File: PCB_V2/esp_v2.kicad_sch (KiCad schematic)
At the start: 13 parts, among them J2 Conn_01x03_Socket, J3 Screw_Terminal_01x02, U1 ESP-32S

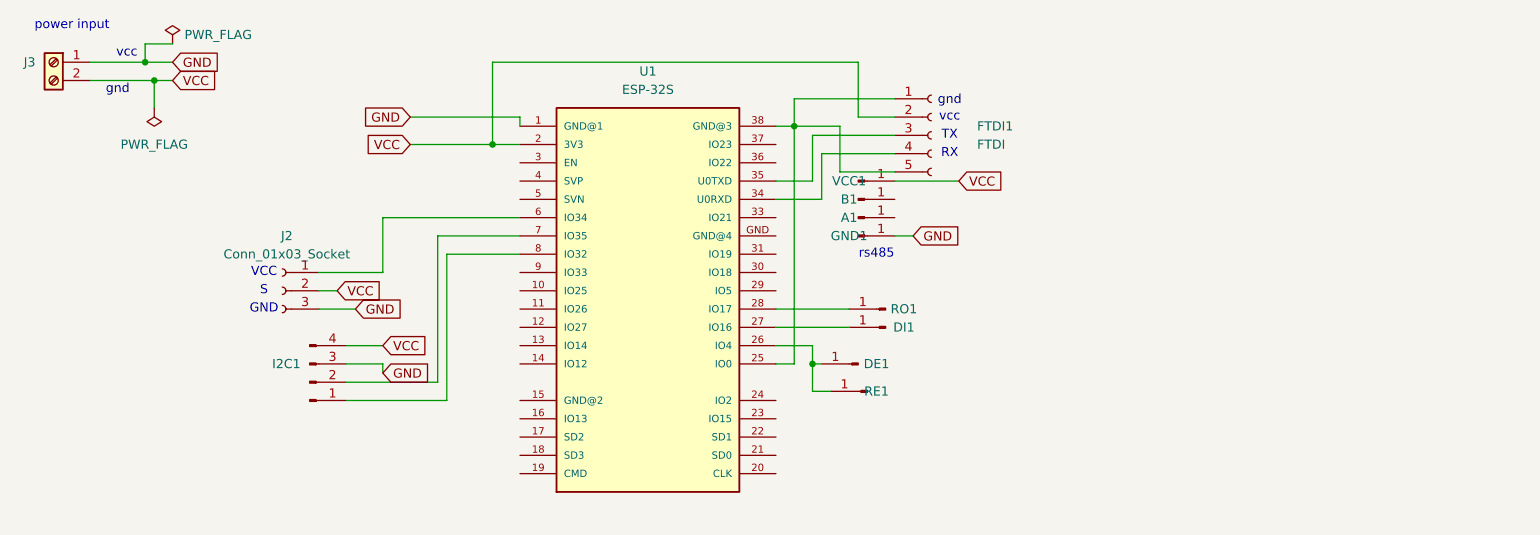
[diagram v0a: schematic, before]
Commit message: expanded tracks' width
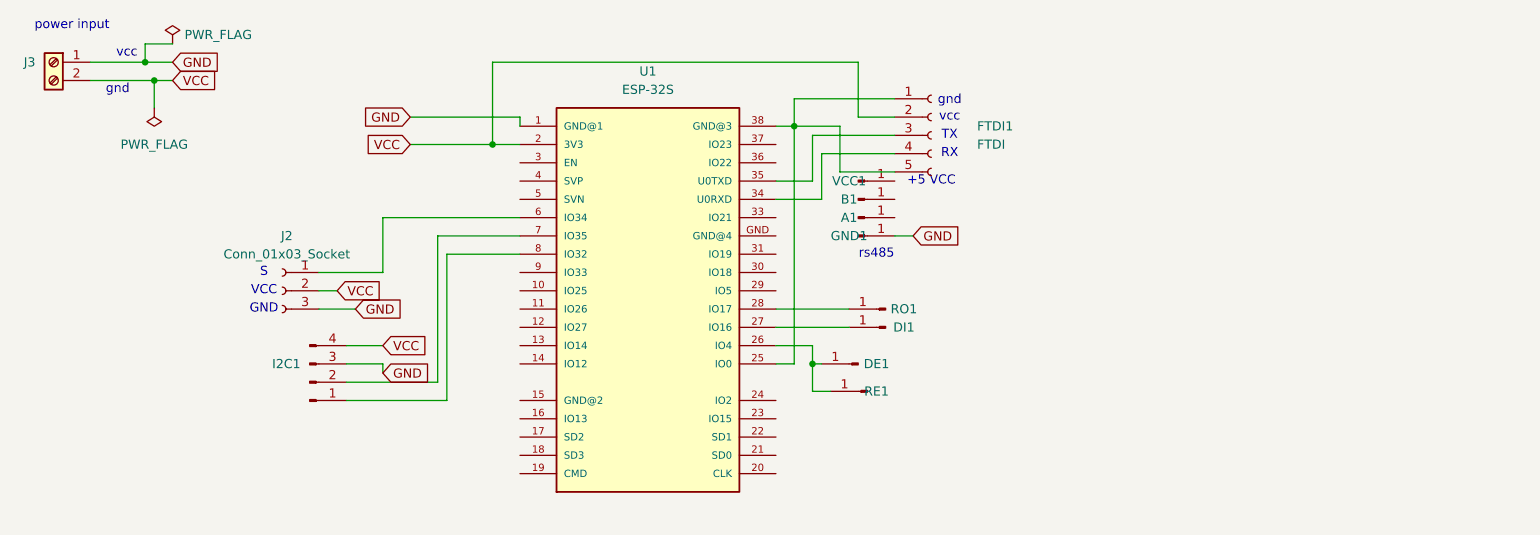
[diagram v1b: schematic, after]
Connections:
- net VCC: no longer VCC1.1 (Pin_1)
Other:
- note added: "+5 VCC"
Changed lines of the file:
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@@
 	(generator_version "9.0")
 	(paper "A4")
-	(text "VCC\n"
+	(text "S"
 		(exclude_from_sim no)
 		(at 50.8 48.26 0)
@@
 		)
 	)
-	(text "S\n"
+	(text "+5 VCC"
+		(exclude_from_sim no)
+		(at 143.51 35.56 0)
+		(effects
+			(font
+				(size 1.27 1.27)
+			)
+		)
+	)
+	(text "VCC"
 		(exclude_from_sim no)
 		(at 50.8 50.8 0)
@@
 	(wire
 		(pts
-			(xy 138.43 35.56) (xy 147.32 35.56)
-		)
-		(stroke
-			(width 0)
-			(type default)
-		)
-	)
-	(wire
-		(pts
 			(xy 38.1 16.51) (xy 34.29 16.51)
 		)
@@
 				(hide yes)
 			)
-		)
-	)
-	(global_label "VCC"
-		(shape input)
-		(at 147.32 35.56 0)
-		(fields_autoplaced yes)
-		(effects
-			(font
-				(size 1.27 1.27)
-			)
-			(justify left)
-		)
-		(property "Intersheetrefs" "${INTERSHEET_REFS}"
-			(at 153.9338 35.56 0)
-			(effects
-				(font
-					(size 1.27 1.27)
-				)
-				(justify left)
-				(hide yes)
-			)

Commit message: After our first etching we reiliaze pins were too small . SO we had toenlearge them.
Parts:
- A1, B1, DE1, GND1, RE1, RO1, VCC1: footprint Connector_PinHeader_1.00mm:PinHeader_1x01_P1.00mm_Vertical -> Connector_PinHeader_2.54mm:PinHeader_1x01_P2.54mm_Vertical
- FTDI1: footprint Connector_PinSocket_1.00mm:PinSocket_1x05_P1.00mm_Vertical -> Connector_PinSocket_2.54mm:PinSocket_1x05_P2.54mm_Vertical
- I2C1: footprint Connector_PinHeader_1.00mm:PinHeader_1x04_P1.00mm_Vertical -> Connector_PinHeader_2.54mm:PinHeader_1x04_P2.54mm_Vertical
- J2: footprint Connector_PinSocket_1.00mm:PinSocket_1x03_P1.00mm_Vertical -> Connector_PinSocket_2.54mm:PinSocket_1x03_P2.54mm_Vertical
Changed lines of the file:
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@@
 			)
 		)
-		(property "Footprint" "Connector_PinHeader_1.00mm:PinHeader_1x01_P1.00mm_Vertical"
+		(property "Footprint" "Connector_PinHeader_2.54mm:PinHeader_1x01_P2.54mm_Vertical"
 			(at 134.62 64.77 0)
 			(effects
@@
 			)
 		)
-		(property "Footprint" "Connector_PinHeader_1.00mm:PinHeader_1x01_P1.00mm_Vertical"
+		(property "Footprint" "Connector_PinHeader_2.54mm:PinHeader_1x01_P2.54mm_Vertical"
 			(at 133.35 40.64 0)
 			(effects
@@
 			)
 		)
-		(property "Footprint" "Connector_PinHeader_1.00mm:PinHeader_1x01_P1.00mm_Vertical"
+		(property "Footprint" "Connector_PinHeader_2.54mm:PinHeader_1x01_P2.54mm_Vertical"
 			(at 133.35 60.96 0)
 			(effects
@@
 			)
 		)
-		(property "Footprint" "Connector_PinHeader_1.00mm:PinHeader_1x04_P1.00mm_Vertical"
+		(property "Footprint" "Connector_PinHeader_2.54mm:PinHeader_1x04_P2.54mm_Vertical"
 			(at 57.15 63.5 0)
 			(effects
@@
 			)
 		)
-		(property "Footprint" "Connector_PinHeader_1.00mm:PinHeader_1x01_P1.00mm_Vertical"
+		(property "Footprint" "Connector_PinHeader_2.54mm:PinHeader_1x01_P2.54mm_Vertical"
 			(at 133.35 35.56 0)
 			(effects
@@
 			)
 		)
-		(property "Footprint" "Connector_PinSocket_1.00mm:PinSocket_1x05_P1.00mm_Vertical"
+		(property "Footprint" "Connector_PinSocket_2.54mm:PinSocket_1x05_P2.54mm_Vertical"
 			(at 143.51 29.21 0)
 			(effects
@@
 			)
 		)
-		(property "Footprint" "Connector_PinHeader_1.00mm:PinHeader_1x01_P1.00mm_Vertical"
+		(property "Footprint" "Connector_PinHeader_2.54mm:PinHeader_1x01_P2.54mm_Vertical"
 			(at 133.35 43.18 0)
 			(effects
@@
 			)
 		)
-		(property "Footprint" "Connector_PinHeader_1.00mm:PinHeader_1x01_P1.00mm_Vertical"
+		(property "Footprint" "Connector_PinHeader_2.54mm:PinHeader_1x01_P2.54mm_Vertical"
 			(at 133.35 38.1 0)
 			(effects
@@
 			)
 		)
-		(property "Footprint" "Connector_PinSocket_1.00mm:PinSocket_1x03_P1.00mm_Vertical"
+		(property "Footprint" "Connector_PinSocket_2.54mm:PinSocket_1x03_P2.54mm_Vertical"
 			(at 53.34 50.8 0)
 			(effects
@@
 			)
 		)
-		(property "Footprint" "Connector_PinHeader_1.00mm:PinHeader_1x01_P1.00mm_Vertical"
+		(property "Footprint" "Connector_PinHeader_2.54mm:PinHeader_1x01_P2.54mm_Vertical"
 			(at 137.16 53.34 0)
 			(effects

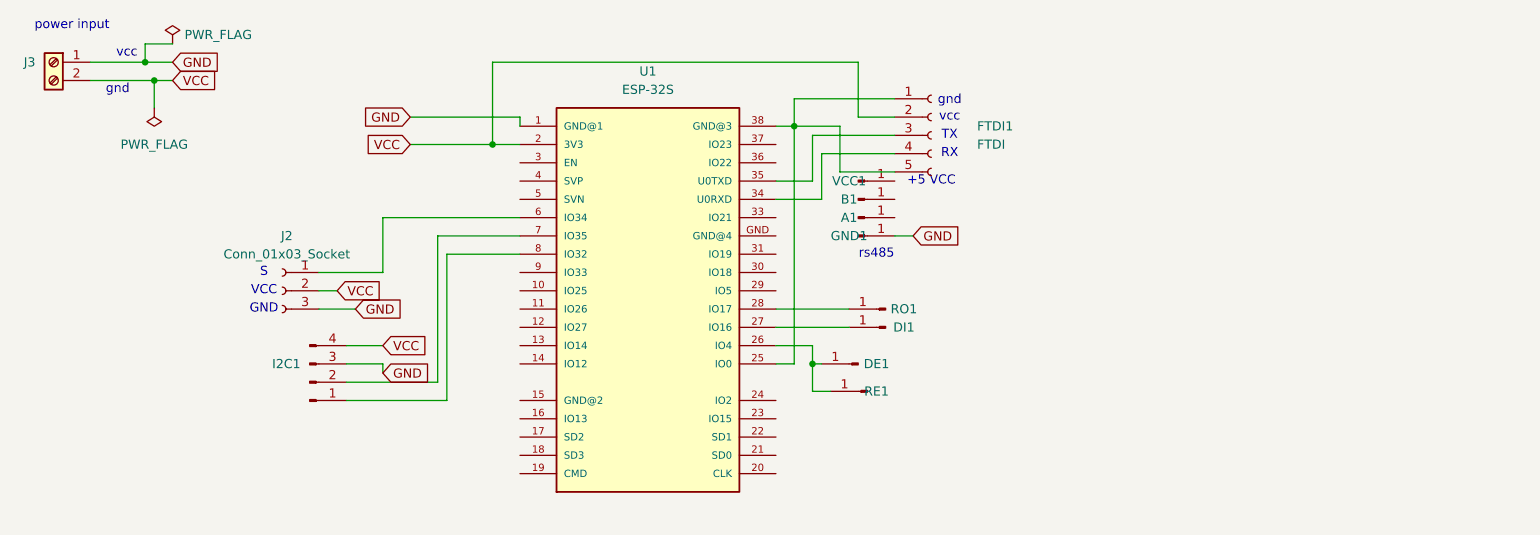
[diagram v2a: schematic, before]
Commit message: correction on I2C for the lcd
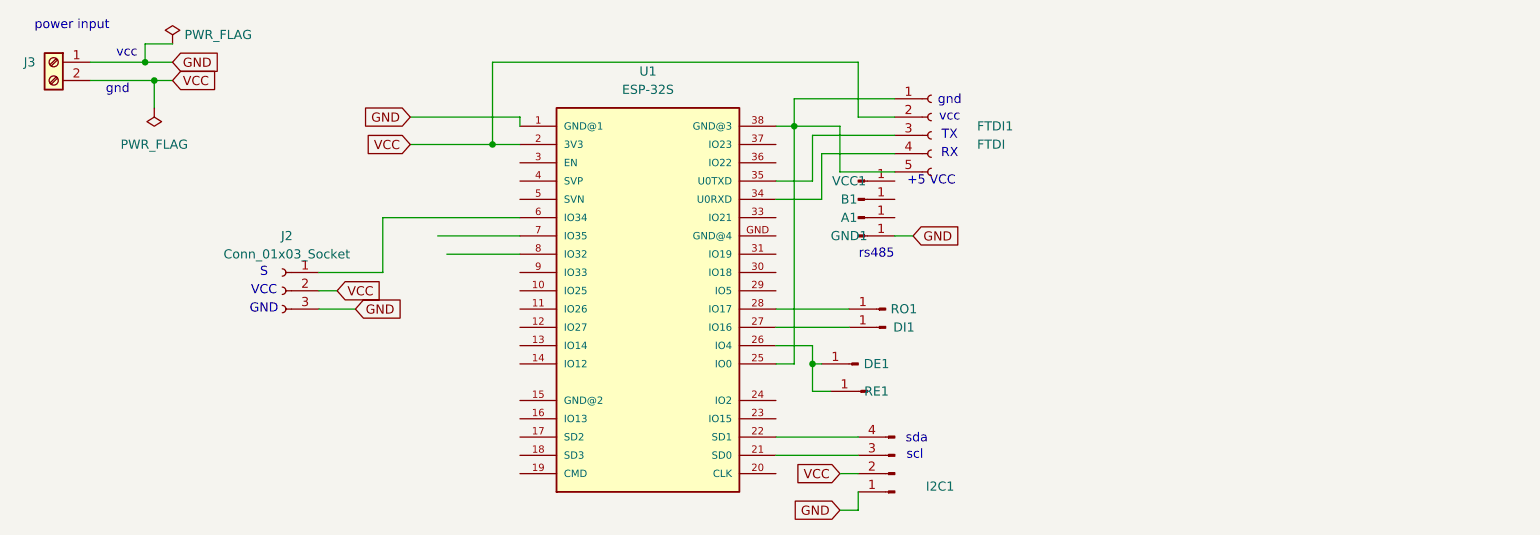
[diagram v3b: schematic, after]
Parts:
- DI1: footprint Connector_PinHeader_1.00mm:PinHeader_1x01_P1.00mm_Vertical -> Connector_PinHeader_2.54mm:PinHeader_1x01_P2.54mm_Vertical
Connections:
- net GND: now also I2C1.1 (Pin_1); no longer I2C1.3 (Pin_3)
- net VCC: now also I2C1.2 (Pin_2); no longer I2C1.4 (Pin_4)
- net at U1.21 (SD0): now also I2C1.3 (Pin_3)
- net at U1.22 (SD1): now also I2C1.4 (Pin_4)
- net at U1.7 (IO35): no longer I2C1.2 (Pin_2)
- net at U1.8 (IO32): no longer I2C1.1 (Pin_1)
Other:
- note added: "scl"
- note added: "sda"
- moved on the sheet: I2C1
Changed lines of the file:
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@@
 	(generator_version "9.0")
 	(paper "A4")
+	(text "sda"
+		(exclude_from_sim no)
+		(at 141.478 71.374 0)
+		(effects
+			(font
+				(size 1.27 1.27)
+			)
+		)
+	)
 	(text "S"
 		(exclude_from_sim no)
@@
 		(exclude_from_sim no)
 		(at 146.05 26.67 0)
+		(effects
+			(font
+				(size 1.27 1.27)
+			)
+		)
+	)
+	(text "scl\n"
+		(exclude_from_sim no)
+		(at 141.224 73.66 0)
 		(effects
 			(font
@@
 	(wire
 		(pts
+			(xy 121.92 73.66) (xy 133.35 73.66)
+		)
+		(stroke
+			(width 0)
+			(type default)
+		)
+	)
+	(wire
+		(pts
 			(xy 26.67 21.59) (xy 35.56 21.59)
 		)
@@
 	(wire
 		(pts
+			(xy 130.81 76.2) (xy 133.35 76.2)
+		)
+		(stroke
+			(width 0)
+			(type default)
+		)
+	)
+	(wire
+		(pts
 			(xy 67.31 40.64) (xy 67.31 48.26)
 		)
@@
 	(wire
 		(pts
-			(xy 67.31 60.96) (xy 67.31 62.23)
-		)
-		(stroke
-			(width 0)
-			(type default)
-		)
-	)
-	(wire
-		(pts
 			(xy 58.42 53.34) (xy 63.5 53.34)
 		)
@@
 	(wire
 		(pts
-			(xy 62.23 66.04) (xy 76.2 66.04)
+			(xy 133.35 81.28) (xy 133.35 78.74)
 		)
 		(stroke
@@
 	(wire
 		(pts
-			(xy 74.93 63.5) (xy 62.23 63.5)
-		)
-		(stroke
-			(width 0)
-			(type default)
-		)
-	)
-	(wire
-		(pts
 			(xy 124.46 27.94) (xy 130.81 27.94)
 		)
@@
 	(wire
 		(pts
-			(xy 62.23 60.96) (xy 67.31 60.96)
-		)
-		(stroke
-			(width 0)
-			(type default)
-		)
-	)
-	(wire
-		(pts
 			(xy 121.92 35.56) (xy 127 35.56)
 		)
@@
 	(wire
 		(pts
-			(xy 76.2 66.04) (xy 76.2 45.72)
+			(xy 130.81 81.28) (xy 133.35 81.28)
 		)
 		(stroke
@@
 	(wire
 		(pts
+			(xy 121.92 71.12) (xy 133.35 71.12)
+		)
+		(stroke
+			(width 0)
+			(type default)
+		)
+	)
+	(wire
+		(pts
 			(xy 35.56 21.59) (xy 35.56 25.4)
 		)
@@
 	(wire
 		(pts
-			(xy 74.93 43.18) (xy 74.93 63.5)
-		)
-		(stroke
-			(width 0)
-			(type default)
-		)
-	)
-	(wire
-		(pts
 			(xy 121.92 60.96) (xy 124.46 60.96)
 		)
@@
 	(wire
 		(pts
-			(xy 62.23 58.42) (xy 67.31 58.42)
-		)
-		(stroke
-			(width 0)
-			(type default)
-		)
-	)
-	(wire
-		(pts
 			(xy 35.56 21.59) (xy 38.1 21.59)
 		)
@@
 			(width 0)
 			(type default)
-		)
-	)
-	(global_label "GND"
-		(shape input)
-		(at 67.31 62.23 0)
-		(fields_autoplaced yes)
-		(effects
-			(font
-				(size 1.27 1.27)
-			)
-			(justify left)
-		)
-		(property "Intersheetrefs" "${INTERSHEET_REFS}"
-			(at 74.1657 62.23 0)
-			(effects
-				(font
-					(size 1.27 1.27)
-				)
-				(justify left)
-				(hide yes)
-			)
 		)
 	)
@@
 		)
 	)
-	(global_label "VCC"
+	(global_label "GND"
 		(shape input)
-		(at 67.31 58.42 0)
+		(at 130.81 81.28 180)
 		(fields_autoplaced yes)
 		(effects
@@
 				(size 1.27 1.27)
 			)
-			(justify left)
+			(justify right)
 		)
 		(property "Intersheetrefs" "${INTERSHEET_REFS}"
-			(at 73.9238 58.42 0)
-			(effects
-				(font
-					(size 1.27 1.27)
-				)
-				(justify left)
+			(at 123.9543 81.28 0)
+			(effects
+				(font
+					(size 1.27 1.27)
+				)
+				(justify right)
 				(hide yes)
 			)
@@
 				)
 				(justify left)
+				(hide yes)
+			)
+		)
+	)
+	(global_label "VCC"
+		(shape input)
+		(at 130.81 76.2 180)
+		(fields_autoplaced yes)
+		(effects
+			(font
+				(size 1.27 1.27)
+			)
+			(justify right)
+		)
+		(property "Intersheetrefs" "${INTERSHEET_REFS}"
+			(at 124.1962 76.2 0)
+			(effects
+				(font
+					(size 1.27 1.27)
+				)
+				(justify right)
 				(hide yes)
 			)
@@
 	(symbol
 		(lib_id "Connector:Conn_01x04_Pin")
-		(at 57.15 63.5 0)
-		(mirror x)
+		(at 138.43 76.2 180)
 		(unit 1)
 		(exclude_from_sim no)
@@
 		(dnp no)
 		(property "Reference" "I2C1"
-			(at 55.88 60.9599 0)
+			(at 142.748 77.978 0)
 			(effects
 				(font
@@
 		)
 		(property "Value" "Conn_01x04_Pin"
-			(at 55.88 63.4999 0)
+			(at 139.7 76.1999 0)
 			(effects
 				(font
@@
 		)
 		(property "Footprint" "Connector_PinHeader_2.54mm:PinHeader_1x04_P2.54mm_Vertical"
-			(at 57.15 63.5 0)
+			(at 138.43 76.2 0)
 			(effects
 				(font
@@
 		)
 		(property "Datasheet" "~"
-			(at 57.15 63.5 0)
+			(at 138.43 76.2 0)
 			(effects
 				(font
@@
 		)
 		(property "Description" "Generic connector, single row, 01x04, script generated"
-			(at 57.15 63.5 0)
+			(at 138.43 76.2 0)
 			(effects
 				(font
@@
 			)
 		)
-		(property "Footprint" "Connector_PinHeader_1.00mm:PinHeader_1x01_P1.00mm_Vertical"
+		(property "Footprint" "Connector_PinHeader_2.54mm:PinHeader_1x01_P2.54mm_Vertical"
 			(at 137.16 55.88 0)
 			(effects

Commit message: added power button
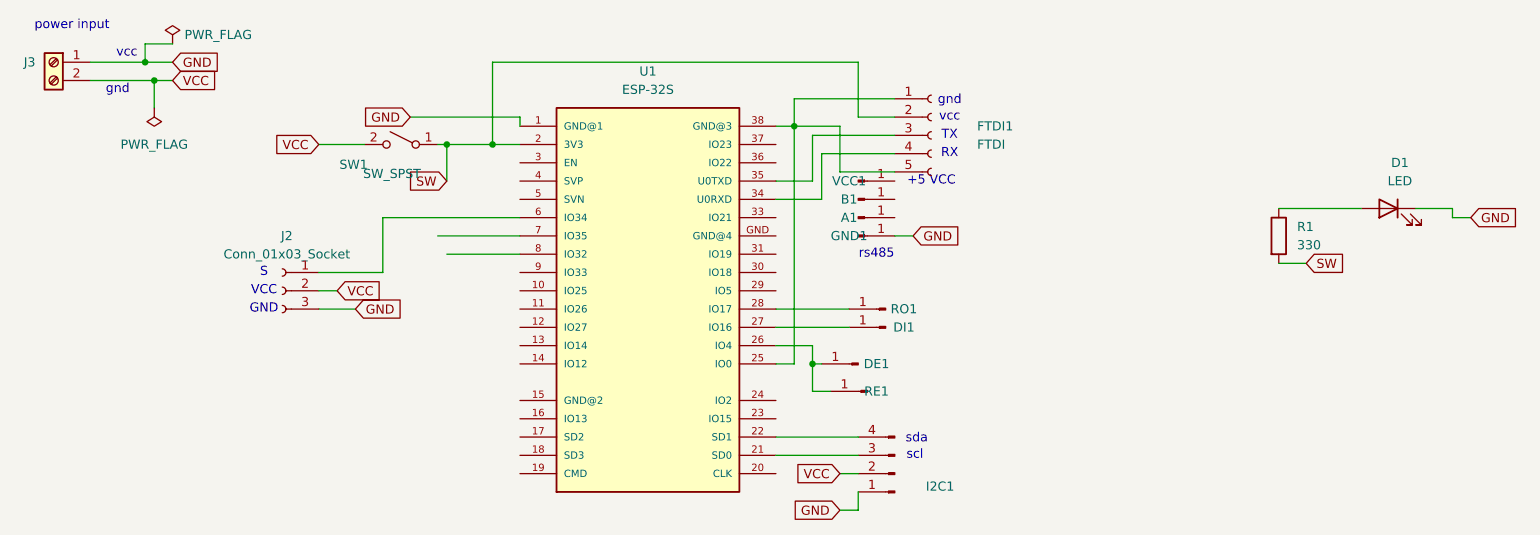
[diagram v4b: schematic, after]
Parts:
- added D1: LED, LED_THT:LED_D1.8mm_W3.3mm_H2.4mm, symbol Device:LED
- added R1: 330, Resistor_SMD:R_0815_2038Metric_Pad1.20x4.05mm_HandSolder, symbol Device:R
- added SW1: SW_SPST, Button_Switch_SMD:SW_DIP_SPSTx01_Slide_6.7x4.1mm_W8.61mm_P2.54mm_LowProfile, symbol Switch:SW_SPST
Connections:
- net GND: now also D1.1 (K)
- net VCC: now also SW1.2 (B); no longer FTDI1.2 (Pin_2), U1.2 (3V3)
- new net: D1.2 (A), R1.1
- new net SW: FTDI1.2 (Pin_2), R1.2, SW1.1 (A), U1.2 (3V3)
